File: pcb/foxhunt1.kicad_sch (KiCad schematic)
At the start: 0 parts

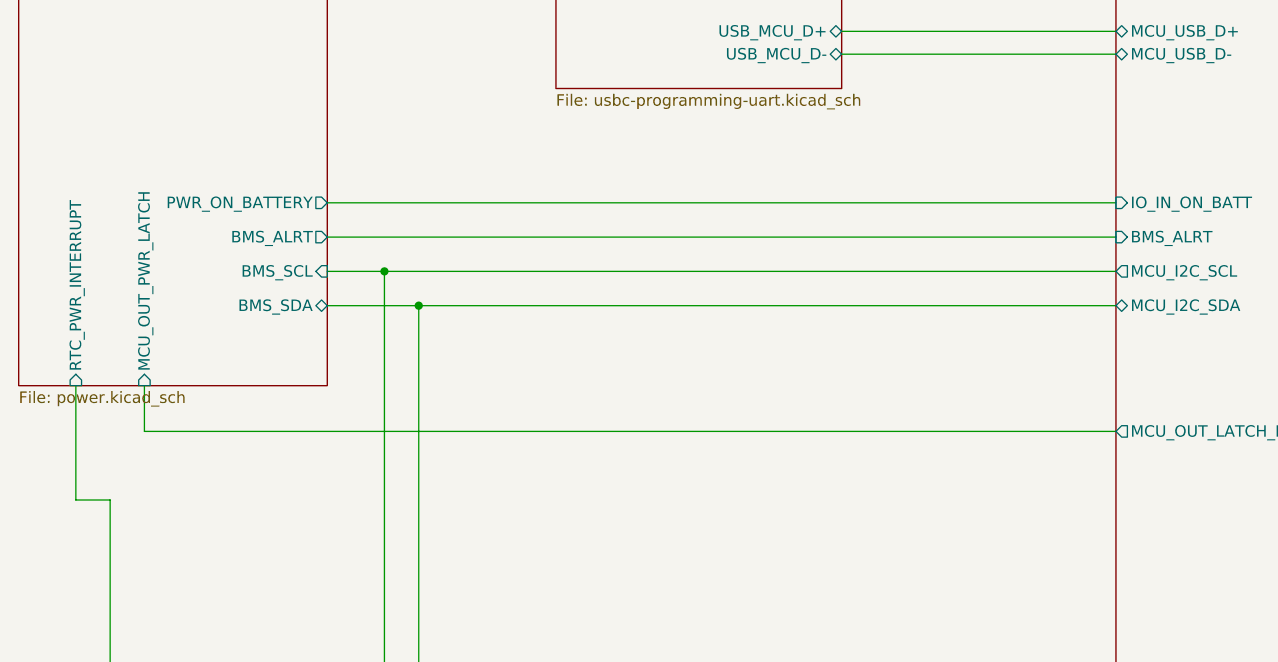
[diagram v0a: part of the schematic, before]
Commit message: fix some drc issues
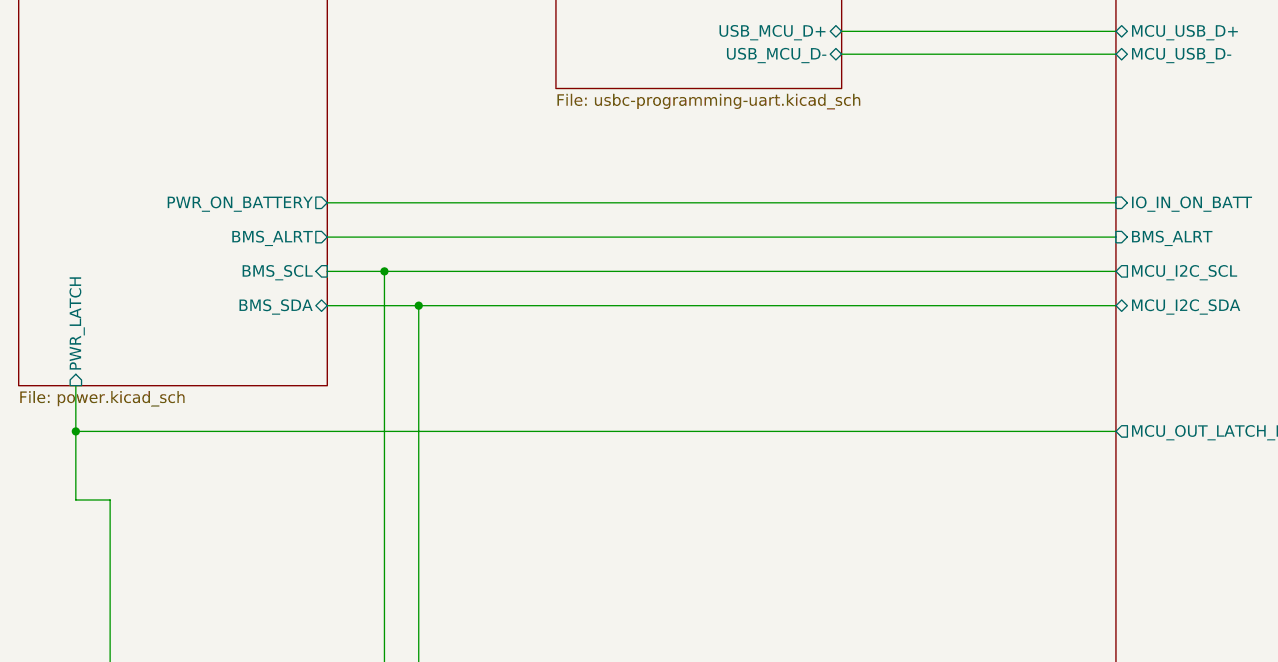
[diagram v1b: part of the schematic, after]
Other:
- sheet Power ports: added PWR_LATCH; removed MCU_OUT_PWR_LATCH, RTC_PWR_INTERRUPT
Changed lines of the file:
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@@
 		(color 0 0 0 0)
 	)
+	(junction
+		(at 50.8 105.41)
+		(diameter 0)
+		(color 0 0 0 0)
+	)
 	(wire
 		(pts
@@
 	(wire
 		(pts
-			(xy 58.42 100.33) (xy 58.42 105.41)
-		)
-		(stroke
-			(width 0)
-			(type default)
-		)
-	)
-	(wire
-		(pts
 			(xy 78.74 91.44) (xy 88.9 91.44)
 		)
@@
 	(wire
 		(pts
-			(xy 50.8 113.03) (xy 50.8 100.33)
+			(xy 50.8 113.03) (xy 50.8 105.41)
 		)
 		(stroke
@@
 	(wire
 		(pts
-			(xy 58.42 105.41) (xy 166.37 105.41)
+			(xy 50.8 105.41) (xy 166.37 105.41)
 		)
 		(stroke
@@
 		(pts
 			(xy 78.74 83.82) (xy 166.37 83.82)
+		)
+		(stroke
+			(width 0)
+			(type default)
+		)
+	)
+	(wire
+		(pts
+			(xy 50.8 105.41) (xy 50.8 100.33)
 		)
 		(stroke
@@
 			)
 		)
-		(pin "MCU_OUT_PWR_LATCH" input
-			(at 58.42 100.33 270)
-			(effects
-				(font
-					(size 1.27 1.27)
-				)
-				(justify left)
-			)
-		)
-		(pin "RTC_PWR_INTERRUPT" input
+		(pin "PWR_LATCH" input
 			(at 50.8 100.33 270)
 			(effects
